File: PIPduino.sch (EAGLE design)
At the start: 41 parts, among them IC1 ATmega328P\, IC2 SPX1117, J1 ISP/SPI

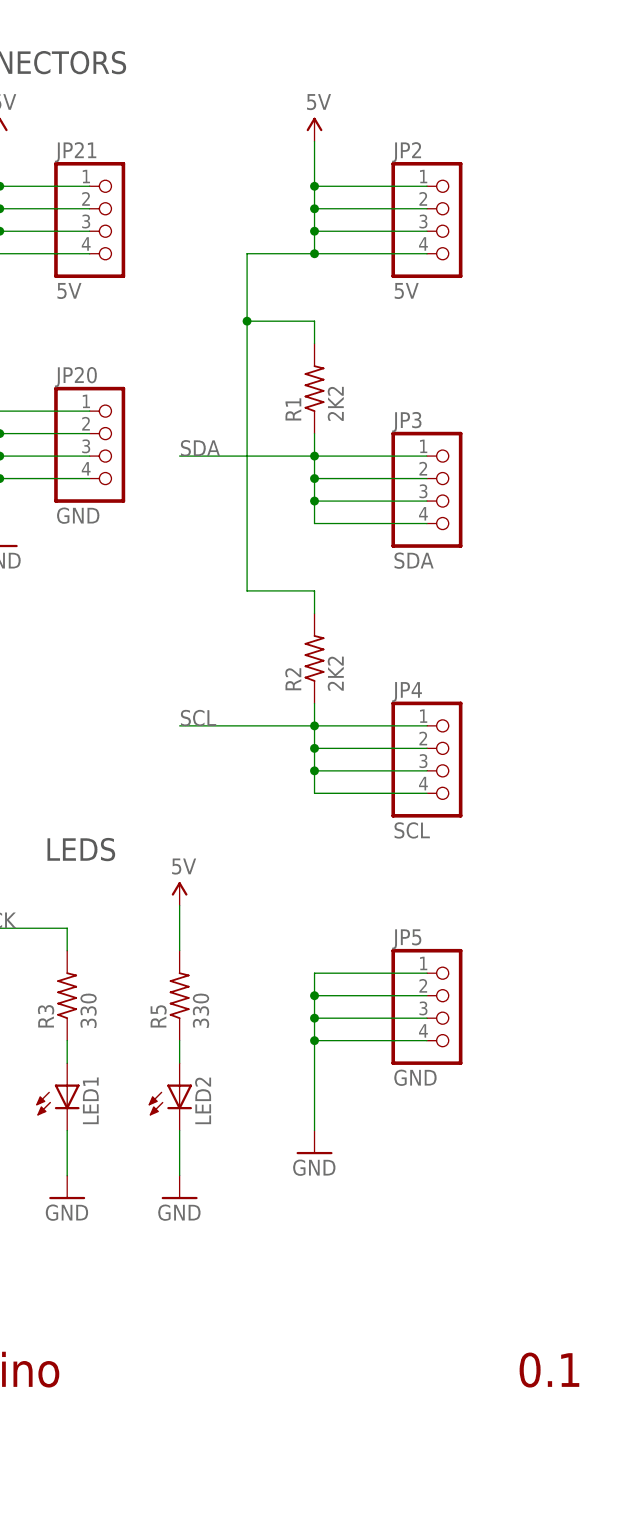
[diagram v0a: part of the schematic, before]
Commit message: Added 5th I2C, fixed silk for VIN
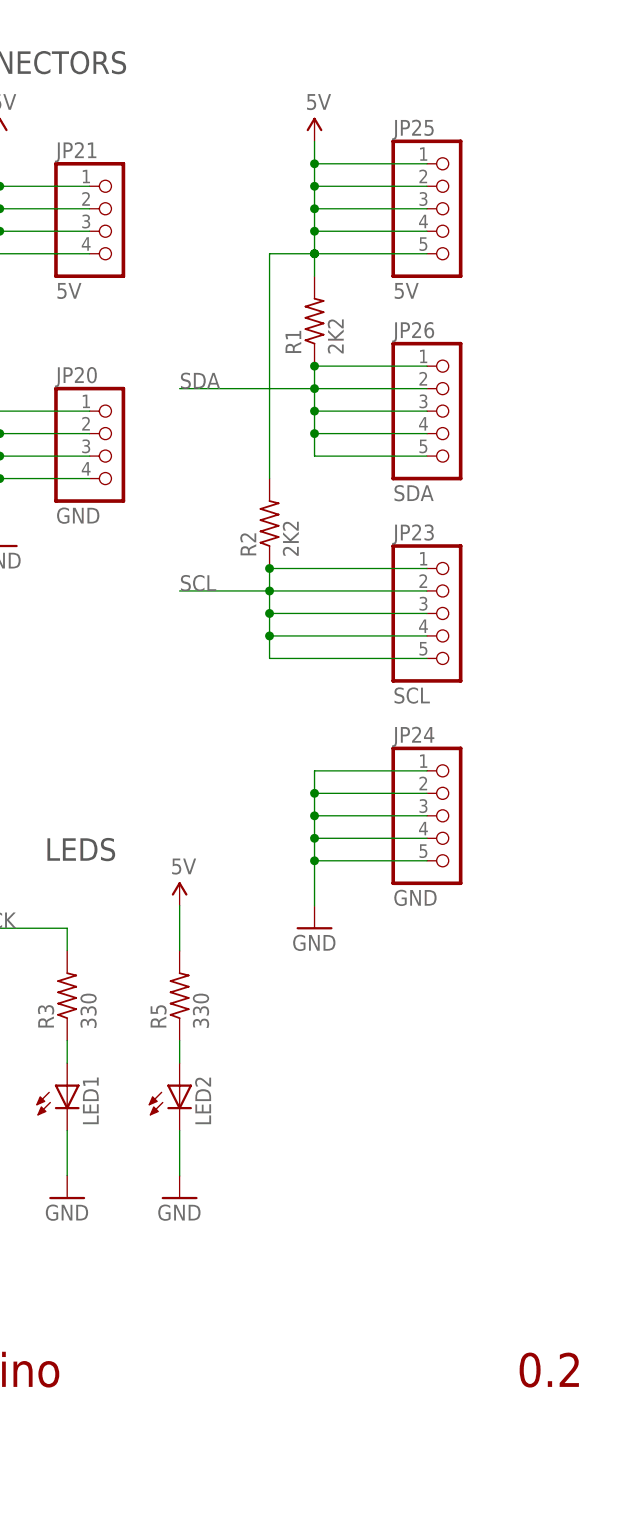
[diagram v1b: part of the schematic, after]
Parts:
- removed JP2: 5V, pinhead-2:PINHD-1X04_2.54-S
- removed JP3: SDA, pinhead-2:PINHD-1X04_2.54-S
- removed JP4: SCL, pinhead-2:PINHD-1X04_2.54-S
- removed JP5: GND, pinhead-2:PINHD-1X04_2.54-S
- added JP23: SCL, pinhead-2:PINHD-1X05_2.54-S
- added JP24: GND, pinhead-2:PINHD-1X05_2.54-S
- added JP25: 5V, pinhead-2:PINHD-1X05_2.54-S
- added JP26: SDA, pinhead-2:PINHD-1X05_2.54-S
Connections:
- net 5V: now also JP25.1, JP25.2, JP25.3, JP25.4, JP25.5; no longer JP2.1, JP2.2, JP2.3, JP2.4
- net GND: now also JP24.1, JP24.2, JP24.3, JP24.4, JP24.5; no longer JP5.1, JP5.2, JP5.3, JP5.4
- net SCL: now also JP23.1, JP23.2, JP23.3, JP23.4, JP23.5; no longer JP4.1, JP4.2, JP4.3, JP4.4
- net SDA: now also JP26.1, JP26.2, JP26.3, JP26.4, JP26.5; no longer JP3.1, JP3.2, JP3.3, JP3.4
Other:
- note added: "0.2"
- note removed: "0.1"
- moved on the sheet: R1, R2

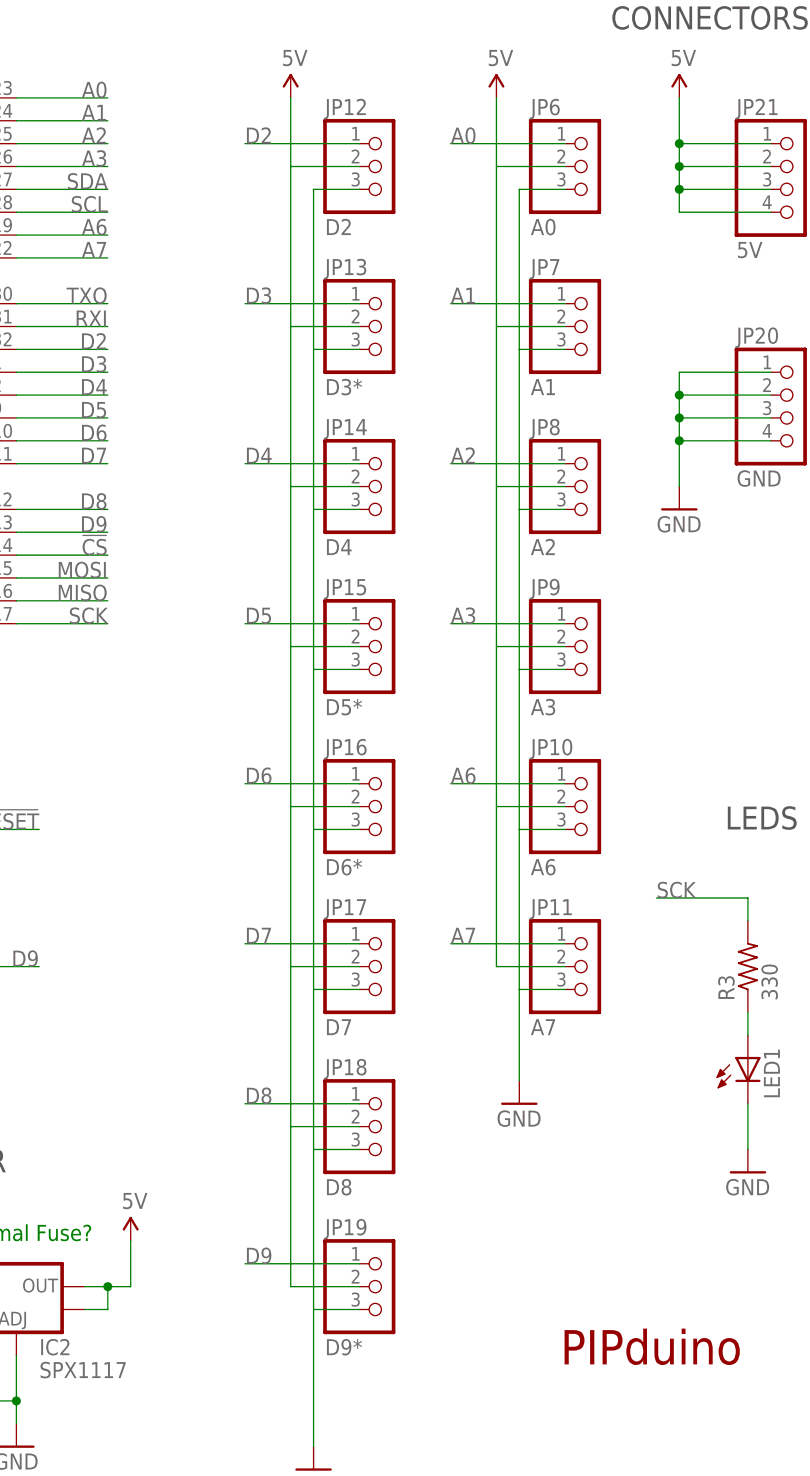
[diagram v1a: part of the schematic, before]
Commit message: Surrounded top screw holes with GND
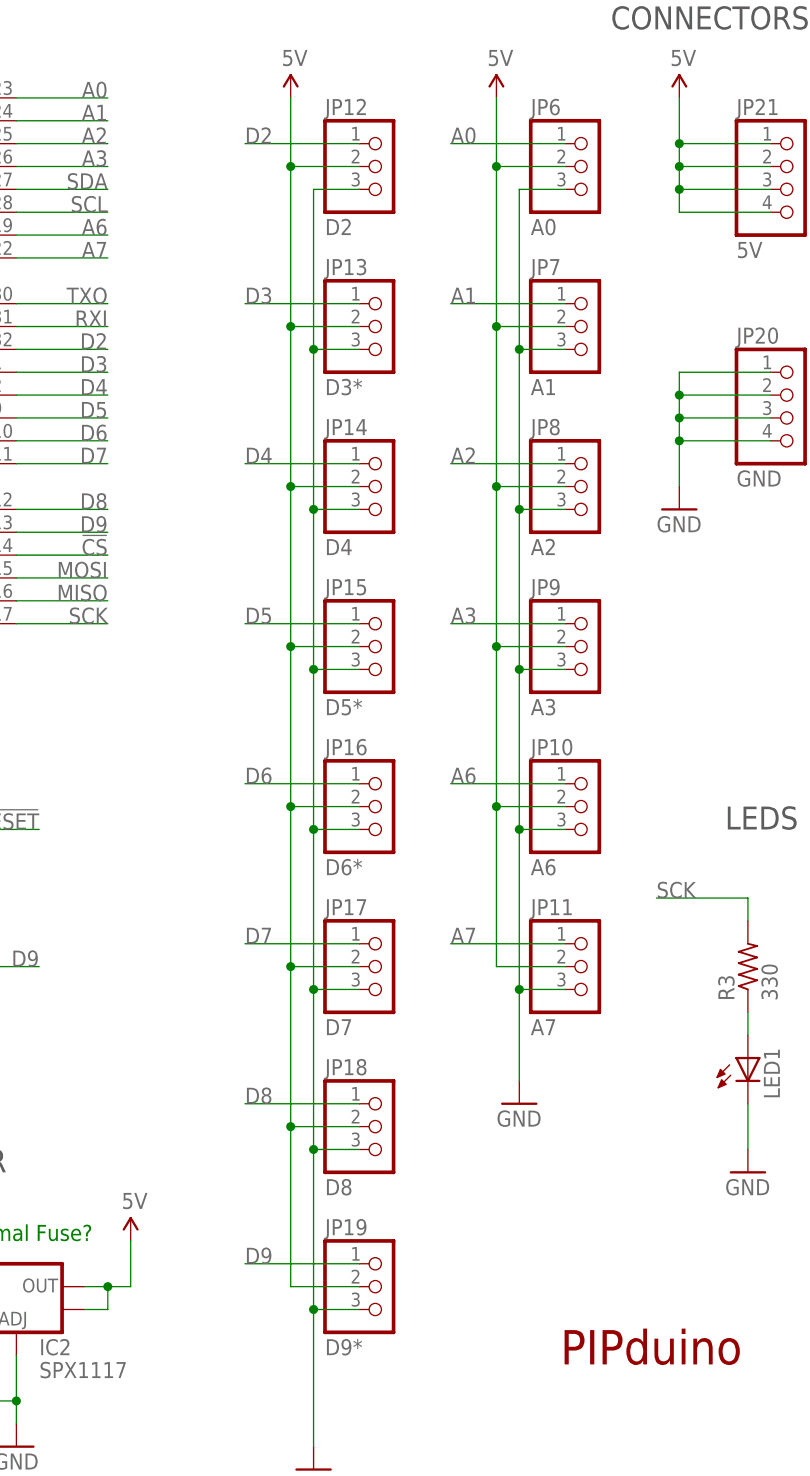
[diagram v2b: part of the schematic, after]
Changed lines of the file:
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@@
 <grid distance="0.1" unitdist="inch" unit="inch" style="lines" multiple="1" display="no" altdistance="0.01" altunitdist="inch" altunit="inch"/>
 <layers>
-<layer number="1" name="Top" color="4" fill="1" visible="yes" active="no"/>
-<layer number="16" name="Bottom" color="1" fill="1" visible="yes" active="no"/>
-<layer number="17" name="Pads" color="2" fill="1" visible="yes" active="no"/>
-<layer number="18" name="Vias" color="2" fill="1" visible="yes" active="no"/>
-<layer number="19" name="Unrouted" color="6" fill="1" visible="yes" active="no"/>
-<layer number="20" name="Dimension" color="15" fill="1" visible="yes" active="no"/>
-<layer number="21" name="tPlace" color="7" fill="1" visible="yes" active="no"/>
-<layer number="22" name="bPlace" color="7" fill="1" visible="yes" active="no"/>
-<layer number="23" name="tOrigins" color="15" fill="1" visible="yes" active="no"/>
-<layer number="24" name="bOrigins" color="15" fill="1" visible="yes" active="no"/>
-<layer number="25" name="tNames" color="7" fill="1" visible="yes" active="no"/>
-<layer number="26" name="bNames" color="7" fill="1" visible="yes" active="no"/>
-<layer number="27" name="tValues" color="7" fill="1" visible="yes" active="no"/>
-<layer number="28" name="bValues" color="7" fill="1" visible="yes" active="no"/>
+<layer number="1" name="Top" color="4" fill="1" visible="no" active="no"/>
+<layer number="16" name="Bottom" color="1" fill="1" visible="no" active="no"/>
+<layer number="17" name="Pads" color="2" fill="1" visible="no" active="no"/>
+<layer number="18" name="Vias" color="2" fill="1" visible="no" active="no"/>
+<layer number="19" name="Unrouted" color="6" fill="1" visible="no" active="no"/>
+<layer number="20" name="Dimension" color="15" fill="1" visible="no" active="no"/>
+<layer number="21" name="tPlace" color="7" fill="1" visible="no" active="no"/>
+<layer number="22" name="bPlace" color="7" fill="1" visible="no" active="no"/>
+<layer number="23" name="tOrigins" color="15" fill="1" visible="no" active="no"/>
+<layer number="24" name="bOrigins" color="15" fill="1" visible="no" active="no"/>
+<layer number="25" name="tNames" color="7" fill="1" visible="no" active="no"/>
+<layer number="26" name="bNames" color="7" fill="1" visible="no" active="no"/>
+<layer number="27" name="tValues" color="7" fill="1" visible="no" active="no"/>
+<layer number="28" name="bValues" color="7" fill="1" visible="no" active="no"/>
 <layer number="29" name="tStop" color="7" fill="3" visible="no" active="no"/>
 <layer number="30" name="bStop" color="7" fill="6" visible="no" active="no"/>
@@
 <layer number="35" name="tGlue" color="7" fill="4" visible="no" active="no"/>
 <layer number="36" name="bGlue" color="7" fill="5" visible="no" active="no"/>
-<layer number="37" name="tTest" color="7" fill="1" visible="yes" active="no"/>
-<layer number="38" name="bTest" color="7" fill="1" visible="yes" active="no"/>
+<layer number="37" name="tTest" color="7" fill="1" visible="no" active="no"/>
+<layer number="38" name="bTest" color="7" fill="1" visible="no" active="no"/>
 <layer number="39" name="tKeepout" color="4" fill="11" visible="no" active="no"/>
 <layer number="40" name="bKeepout" color="1" fill="11" visible="no" active="no"/>
@@
 <layer number="44" name="Drills" color="7" fill="1" visible="no" active="no"/>
 <layer number="45" name="Holes" color="7" fill="1" visible="no" active="no"/>
-<layer number="46" name="Milling" color="3" fill="1" visible="yes" active="no"/>
-<layer number="47" name="Measures" color="7" fill="1" visible="yes" active="no"/>
-<layer number="48" name="Document" color="7" fill="1" visible="yes" active="no"/>
-<layer number="49" name="Reference" color="7" fill="1" visible="yes" active="no"/>
-<layer number="50" name="dxf" color="7" fill="1" visible="yes" active="no"/>
-<layer number="51" name="tDocu" color="7" fill="1" visible="yes" active="no"/>
-<layer number="52" name="bDocu" color="7" fill="1" visible="yes" active="no"/>
-<layer number="53" name="tPadExt" color="7" fill="1" visible="yes" active="no"/>
-<layer number="54" name="bPadExt" color="1" fill="1" visible="yes" active="no"/>
-<layer number="56" name="wert" color="7" fill="1" visible="yes" active="no"/>
+<layer number="46" name="Milling" color="3" fill="1" visible="no" active="no"/>
+<layer number="47" name="Measures" color="7" fill="1" visible="no" active="no"/>
+<layer number="48" name="Document" color="7" fill="1" visible="no" active="no"/>
+<layer number="49" name="Reference" color="7" fill="1" visible="no" active="no"/>
+<layer number="50" name="dxf" color="7" fill="1" visible="no" active="no"/>
+<layer number="51" name="tDocu" color="7" fill="1" visible="no" active="no"/>
+<layer number="52" name="bDocu" color="7" fill="1" visible="no" active="no"/>
+<layer number="53" name="tPadExt" color="7" fill="1" visible="no" active="no"/>
+<layer number="54" name="bPadExt" color="1" fill="1" visible="no" active="no"/>
+<layer number="56" name="wert" color="7" fill="1" visible="no" active="no"/>
 <layer number="91" name="Nets" color="2" fill="1" visible="yes" active="yes"/>
 <layer number="92" name="Busses" color="1" fill="1" visible="yes" active="yes"/>
@@
 <pinref part="JP11" gate="A" pin="3"/>
 <wire x1="160.02" y1="66.04" x2="154.94" y2="66.04" width="0.1524" layer="91"/>
+<junction x="154.94" y="66.04"/>
+<junction x="154.94" y="83.82"/>
+<junction x="154.94" y="101.6"/>
+<junction x="154.94" y="119.38"/>
+<junction x="154.94" y="137.16"/>
 </segment>
 <segment>
@@
 <pinref part="JP19" gate="A" pin="3"/>
 <wire x1="137.16" y1="30.48" x2="132.08" y2="30.48" width="0.1524" layer="91"/>
+<junction x="132.08" y="30.48"/>
+<junction x="132.08" y="48.26"/>
+<junction x="132.08" y="66.04"/>
+<junction x="132.08" y="83.82"/>
+<junction x="132.08" y="101.6"/>
+<junction x="132.08" y="119.38"/>
+<junction x="132.08" y="137.16"/>
 </segment>
 <segment>
@@
 <wire x1="160.02" y1="68.58" x2="152.4" y2="68.58" width="0.1524" layer="91"/>
 <wire x1="152.4" y1="68.58" x2="152.4" y2="86.36" width="0.1524" layer="91"/>
+<junction x="152.4" y="86.36"/>
+<junction x="152.4" y="104.14"/>
+<junction x="152.4" y="121.92"/>
+<junction x="152.4" y="139.7"/>
+<junction x="152.4" y="157.48"/>
 </segment>
 <segment>
@@
 <wire x1="137.16" y1="33.02" x2="129.54" y2="33.02" width="0.1524" layer="91"/>
 <wire x1="129.54" y1="33.02" x2="129.54" y2="50.8" width="0.1524" layer="91"/>
-</segment>
-<segment>
+<junction x="129.54" y="50.8"/>
+<junction x="129.54" y="68.58"/>
+<junction x="129.54" y="86.36"/>
+<junction x="129.54" y="104.14"/>
+<junction x="129.54" y="121.92"/>
+<junction x="129.54" y="139.7"/>
+<junction x="129.54" y="157.48"/>
+</segment>
+<segment>
